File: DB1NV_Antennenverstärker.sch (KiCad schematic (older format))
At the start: 36 parts, among them P1 CONN_01X01_Antenne, P2 CONN_01X02, Q1 BF 545A, Q2 BF 199, Q3 BF 324, U1 LM7812ACT

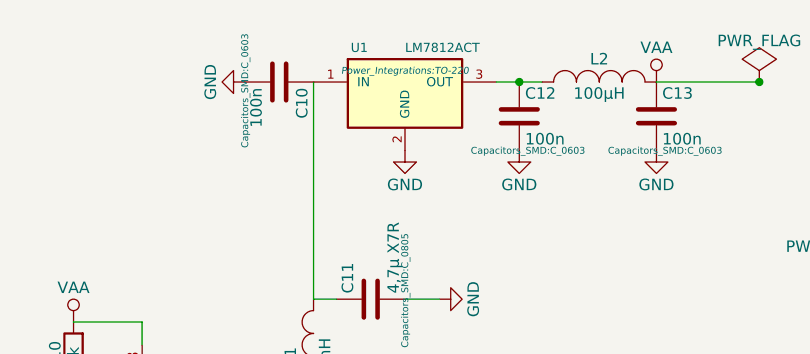
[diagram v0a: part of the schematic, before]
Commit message: Platine v0.1 zum E-Feld Empfänger fertiggestellt.
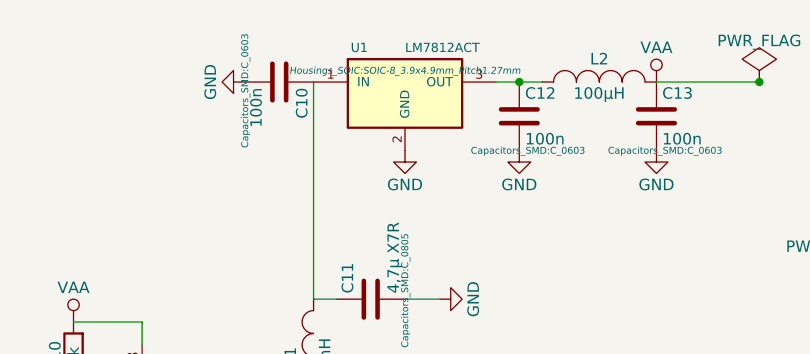
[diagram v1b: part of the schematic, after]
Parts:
- L1, L2: footprint (none) -> lpis2812:L-PIS2812
- U1: footprint Power_Integrations:TO-220 -> Housings_SOIC:SOIC-8_3.9x4.9mm_Pitch1.27mm
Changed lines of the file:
@@
 LIBS:contrib
 LIBS:valves
+LIBS:DB1NV_Antennenverstärker-cache
 EELAYER 25 0
 EELAYER END
@@
 F 0 "L1" H 7750 3700 50  0000 C CNN
 F 1 "1mH" H 7750 3550 50  0000 C CNN
-F 2 "" H 7750 3600 60  0001 C CNN
+F 2 "lpis2812:L-PIS2812" H 7750 3600 60  0001 C CNN
 F 3 "" H 7750 3600 60  0000 C CNN
 F 4 "L-PIS2812" H 7750 3600 60  0001 C CNN "Bauform"
@@
 F 0 "L2" H 9000 2500 50  0000 C CNN
 F 1 "100µH" H 9000 2350 50  0000 C CNN
-F 2 "" H 9000 2400 60  0001 C CNN
+F 2 "lpis2812:L-PIS2812" H 9000 2400 60  0001 C CNN
 F 3 "" H 9000 2400 60  0000 C CNN
 F 4 "L-PIS2812" H 9000 2400 60  0001 C CNN "Bauform"
@@
 F 0 "U1" H 7950 2650 40  0000 C CNN
 F 1 "LM7812ACT" H 8150 2650 40  0000 L CNN
-F 2 "Power_Integrations:TO-220" H 8150 2550 30  0000 C CIN
+F 2 "Housings_SOIC:SOIC-8_3.9x4.9mm_Pitch1.27mm" H 8150 2550 30  0000 C CIN
 F 3 "" H 8150 2450 60  0000 C CNN
 	1    8150 2450
@@
 $EndComp
 $Comp
-L GND #PWR018
+L GND #PWR017
 U 1 1 558375F6
 P 3100 4950
-F 0 "#PWR018" H 3100 4700 50  0001 C CNN
+F 0 "#PWR017" H 3100 4700 50  0001 C CNN
 F 1 "GND" H 3100 4800 50  0000 C CNN
 F 2 "" H 3100 4950 60  0000 C CNN
@@
 $EndComp
 $Comp
-L PWR_FLAG #FLG019
+L PWR_FLAG #FLG018
 U 1 1 55837A31
 P 10000 3300
-F 0 "#FLG019" H 10000 3395 50  0001 C CNN
+F 0 "#FLG018" H 10000 3395 50  0001 C CNN
 F 1 "PWR_FLAG" H 10000 3480 50  0000 C CNN
 F 2 "" H 10000 3300 60  0000 C CNN
@@
 $EndComp
 $Comp
-L GND #PWR020
+L GND #PWR019
 U 1 1 55837AB5
 P 10000 3300
-F 0 "#PWR020" H 10000 3050 50  0001 C CNN
+F 0 "#PWR019" H 10000 3050 50  0001 C CNN
 F 1 "GND" H 10000 3150 50  0000 C CNN
 F 2 "" H 10000 3300 60  0000 C CNN
@@
 $EndComp
 $Comp
-L GND #PWR021
+L GND #PWR020
 U 1 1 55837BE5
 P 8100 4400
-F 0 "#PWR021" H 8100 4150 50  0001 C CNN
+F 0 "#PWR020" H 8100 4150 50  0001 C CNN
 F 1 "GND" H 8100 4250 50  0000 C CNN
 F 2 "" H 8100 4400 60  0000 C CNN
@@
 $EndComp
 $Comp
-L VAA #PWR022
+L VAA #PWR021
 U 1 1 5583806A
 P 9250 2400
-F 0 "#PWR022" H 9250 2250 50  0001 C CNN
+F 0 "#PWR021" H 9250 2250 50  0001 C CNN
 F 1 "VAA" H 9250 2550 50  0000 C CNN
 F 2 "" H 9250 2400 60  0000 C CNN
@@
 $EndComp
 $Comp
-L PWR_FLAG #FLG023
+L PWR_FLAG #FLG022
 U 1 1 5583820C
 P 9700 2400
-F 0 "#FLG023" H 9700 2495 50  0001 C CNN
+F 0 "#FLG022" H 9700 2495 50  0001 C CNN
 F 1 "PWR_FLAG" H 9700 2580 50  0000 C CNN
 F 2 "" H 9700 2400 60  0000 C CNN

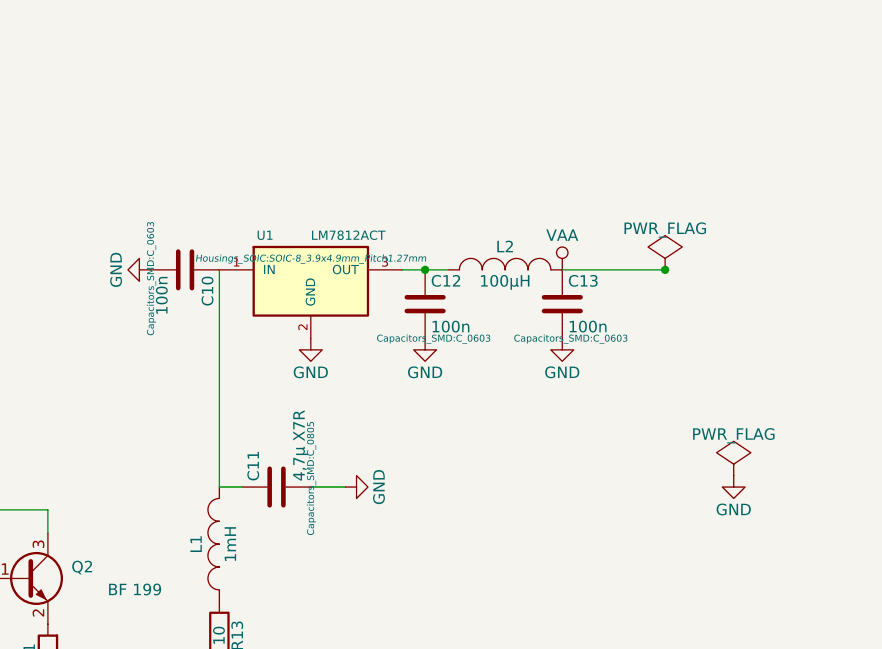
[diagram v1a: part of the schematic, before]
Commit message: Hinzufügen des LT3042 zum Schaltplan (Werte der externen Beschaltung noch nicht berechnet)
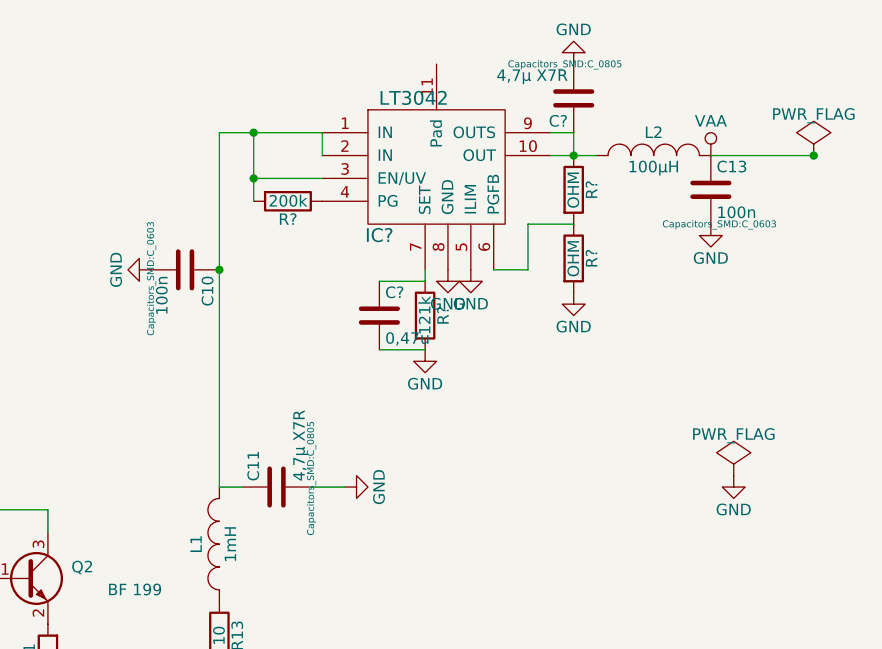
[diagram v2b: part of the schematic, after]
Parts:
- removed C12: 100n, Capacitors_SMD:C_0603, symbol C
- removed U1: LM7812ACT, Housings_SOIC:SOIC-8_3.9x4.9mm_Pitch1.27mm, symbol LM7812ACT
- added C?: 0,47u, symbol C
- added C?: 4,7µ X7R, Capacitors_SMD:C_0805, symbol C
- added IC?: LT3042, symbol LT3042
- added R?: 200k, symbol R
- added R?: 121k, symbol R
- added R? (x2): OHM, symbol R
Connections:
- net GND: now also C?.2, C?.2, IC?.5 (ILIM), IC?.8 (GND), R?.2, R?.2
- net at C10.1, C11.1, L1.2: now also IC?.1 (IN), IC?.2 (IN), IC?.3 (EN/UV), R?.2
- net at L2.1: now also C?.1, IC?.10 (OUT), IC?.9 (OUTS), R?.1
- new net: IC?.4 (PG), R?.1
- new net: IC?.6 (PGFB), R?.1, R?.2
- new net: C?.1, IC?.7 (SET), R?.1
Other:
- moved on the sheet: C13, L2

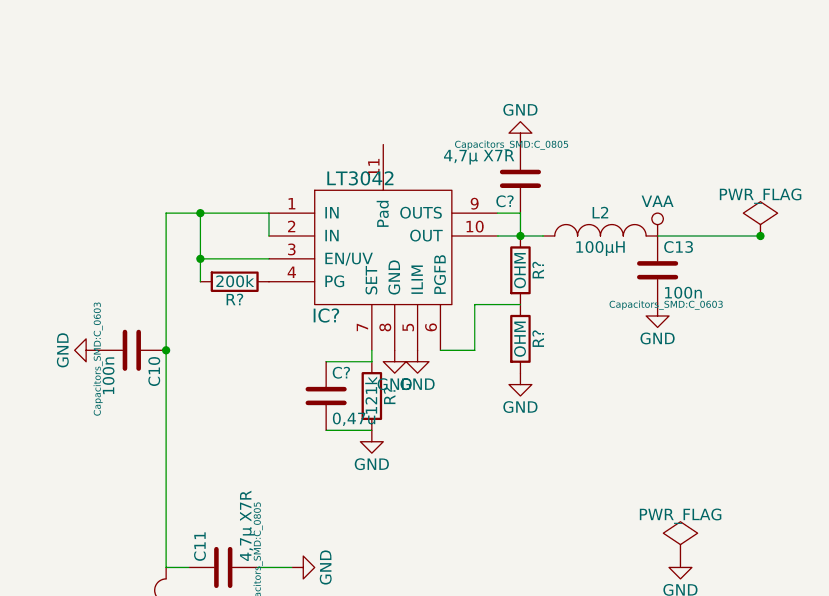
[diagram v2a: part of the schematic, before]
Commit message: Anpassung der Werte des LT3042 Optimierung für Minimales Rauschen (längeres Startup) Undervoltage Threshold  = 10.02 V Power Good Threshold = 11.8 V
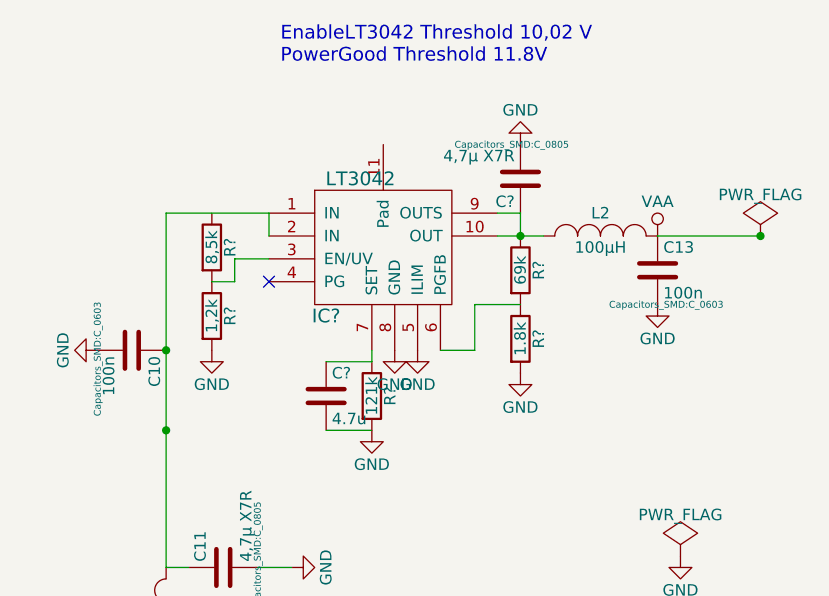
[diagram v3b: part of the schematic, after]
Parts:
- removed R?: 200k, symbol R
- added R?: 1,2k, symbol R
- added R?: 8,5k, symbol R
- C?: value 0,47u -> 4.7u
- R?: value OHM -> 69k
- R?: value OHM -> 1.8k
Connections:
- net GND: now also R?.2
- net at C10.1, C11.1, IC?.1 (IN)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: no longer IC?.3 (EN/UV)
- new net: IC?.3 (EN/UV), R?.1, R?.2
- no-connect marks 0 -> 1
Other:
- note added: "EnableLT3042 Threshold 10,02 V\nPowerGood Threshold 11.8V"
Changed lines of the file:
@@
 Connection ~ 7750 2400
-$Comp
-L R R?
-U 1 1 558D7F66
-P 8050 2100
-F 0 "R?" V 8130 2100 50  0000 C CNN
-F 1 "200k" V 8050 2100 50  0000 C CNN
-F 2 "" V 7980 2100 30  0000 C CNN
-F 3 "" H 8050 2100 30  0000 C CNN
-	1    8050 2100
-	0    1    1    0
-$EndComp
-Wire Wire Line
-	8200 2000 7900 2000
-Wire Wire Line
-	7900 1800 7900 2100
-Connection ~ 7900 1800
-Connection ~ 7900 2000
 $Comp
 L GND #PWR?
@@
 P 8450 2600
 F 0 "C?" H 8475 2700 50  0000 L CNN
-F 1 "0,47u" H 8475 2500 50  0000 L CNN
+F 1 "4.7u" H 8475 2500 50  0000 L CNN
 F 2 "" H 8488 2450 30  0000 C CNN
 F 3 "" H 8450 2600 60  0000 C CNN
@@
 P 9300 2050
 F 0 "R?" V 9380 2050 50  0000 C CNN
-F 1 "OHM" V 9300 2050 50  0000 C CNN
+F 1 "69k" V 9300 2050 50  0000 C CNN
 F 2 "" V 9230 2050 30  0000 C CNN
 F 3 "" H 9300 2050 30  0000 C CNN
@@
 P 9300 2350
 F 0 "R?" V 9380 2350 50  0000 C CNN
-F 1 "OHM" V 9300 2350 50  0000 C CNN
+F 1 "1.8k" V 9300 2350 50  0000 C CNN
 F 2 "" V 9230 2350 30  0000 C CNN
 F 3 "" H 9300 2350 30  0000 C CNN
@@
 Wire Wire Line
 	9100 2400 8950 2400
+$Comp
+L R R?
+U 1 1 558E5880
+P 7950 2250
+F 0 "R?" V 8030 2250 50  0000 C CNN
+F 1 "1,2k" V 7950 2250 50  0000 C CNN
+F 2 "" V 7880 2250 30  0000 C CNN
+F 3 "" H 7950 2250 30  0000 C CNN
+	1    7950 2250
+	1    0    0    -1
+$EndComp
+$Comp
+L R R?
+U 1 1 558E5960
+P 7950 1950
+F 0 "R?" V 8030 1950 50  0000 C CNN
+F 1 "8,5k" V 7950 1950 50  0000 C CNN
+F 2 "" V 7880 1950 30  0000 C CNN
+F 3 "" H 7950 1950 30  0000 C CNN
+	1    7950 1950
+	1    0    0    -1
+$EndComp
+$Comp
+L GND #PWR?
+U 1 1 558E5B71
+P 7950 2400
+F 0 "#PWR?" H 7950 2150 50  0001 C CNN
+F 1 "GND" H 7950 2250 50  0000 C CNN
+F 2 "" H 7950 2400 60  0000 C CNN
+F 3 "" H 7950 2400 60  0000 C CNN
+	1    7950 2400
+	1    0    0    -1
+$EndComp
+Wire Wire Line
+	7950 2100 8050 2100
+Wire Wire Line
+	8050 2100 8050 2000
+Wire Wire Line
+	8050 2000 8200 2000
+Connection ~ 7750 2750
+NoConn ~ 8200 2100
+Text Notes 8250 1150 0    60   ~ 0
+EnableLT3042 Threshold 10,02 V\nPowerGood Threshold 11.8V
 $EndSCHEMATC

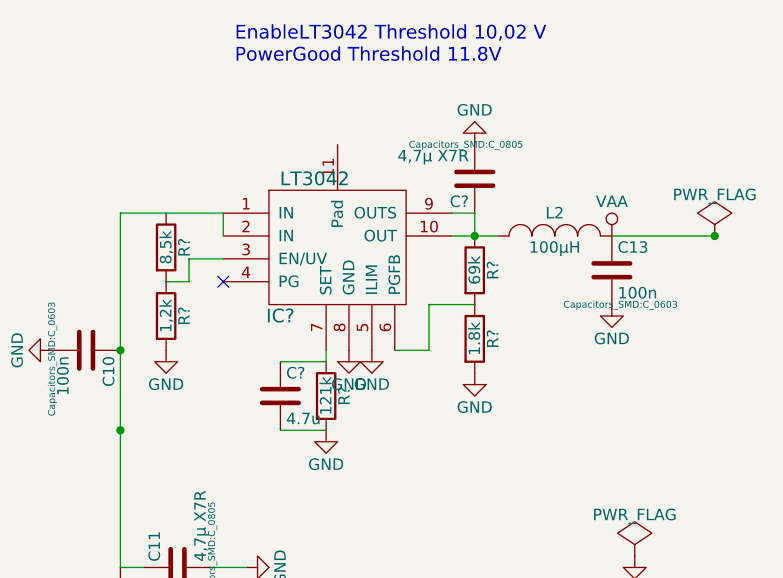
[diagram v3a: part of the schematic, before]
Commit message: Schaltplan leicht modifiziert. eine Spule weniger
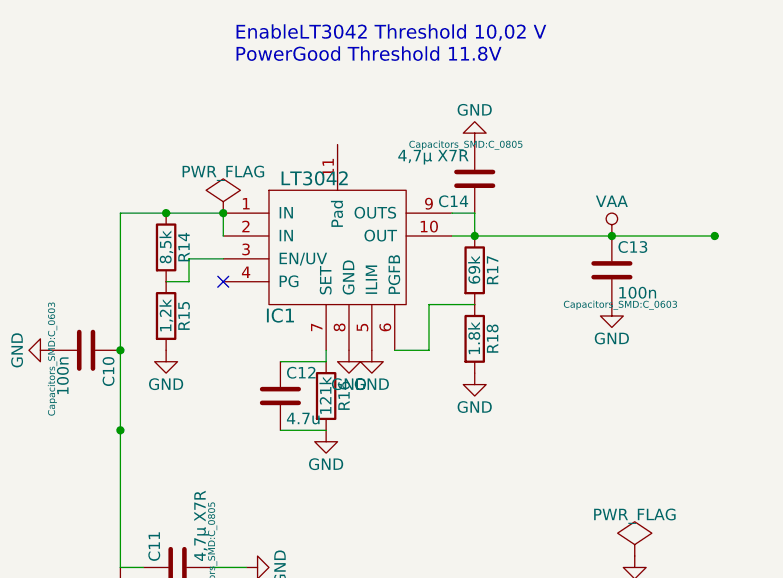
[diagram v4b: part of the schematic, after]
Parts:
- removed L2: 100µH, lpis2812:L-PIS2812, symbol INDUCTOR_SMALL
- gave numbers to parts that had none: 8
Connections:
- net VAA: now also C14.1, IC1.10 (OUT), IC1.9 (OUTS), R17.1
- net at C10.1, C11.1, IC1.1 (IN)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: now also R14.1
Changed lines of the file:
@@
-$EndComp
-$Comp
-L INDUCTOR_SMALL L2
-U 1 1 558344EB
-P 9650 1900
-F 0 "L2" H 9650 2000 50  0000 C CNN
-F 1 "100µH" H 9650 1850 50  0000 C CNN
-F 2 "lpis2812:L-PIS2812" H 9650 1900 60  0001 C CNN
-F 3 "" H 9650 1900 60  0000 C CNN
-F 4 "L-PIS2812" H 9650 1900 60  0001 C CNN "Bauform"
-	1    9650 1900
-	1    0    0    -1
 $EndComp
 $Comp
@@
 $EndComp
 Wire Wire Line
-	9200 1900 9400 1900
+	9200 1900 10350 1900
 Connection ~ 9300 1900
 $Comp
-L GND #PWR015
+L GND #PWR013
 U 1 1 55834F27
 P 7450 2400
-F 0 "#PWR015" H 7450 2150 50  0001 C CNN
+F 0 "#PWR013" H 7450 2150 50  0001 C CNN
 F 1 "GND" H 7450 2250 50  0000 C CNN
 F 2 "" H 7450 2400 60  0000 C CNN
@@
 $EndComp
 $Comp
-L GND #PWR016
+L GND #PWR014
 U 1 1 55835498
 P 9900 2200
-F 0 "#PWR016" H 9900 1950 50  0001 C CNN
+F 0 "#PWR014" H 9900 1950 50  0001 C CNN
 F 1 "GND" H 9900 2050 50  0000 C CNN
 F 2 "" H 9900 2200 60  0000 C CNN
@@
 	1    0    0    -1
 $EndComp
-Wire Wire Line
-	9900 1900 10350 1900
 $Comp
 L ZENER D1
@@
 $EndComp
 $Comp
-L GND #PWR017
+L GND #PWR015
 U 1 1 558375F6
 P 3100 4950
-F 0 "#PWR017" H 3100 4700 50  0001 C CNN
+F 0 "#PWR015" H 3100 4700 50  0001 C CNN
 F 1 "GND" H 3100 4800 50  0000 C CNN
 F 2 "" H 3100 4950 60  0000 C CNN
@@
 $EndComp
 $Comp
-L PWR_FLAG #FLG018
+L PWR_FLAG #FLG016
 U 1 1 55837A31
 P 10000 3300
-F 0 "#FLG018" H 10000 3395 50  0001 C CNN
+F 0 "#FLG016" H 10000 3395 50  0001 C CNN
 F 1 "PWR_FLAG" H 10000 3480 50  0000 C CNN
 F 2 "" H 10000 3300 60  0000 C CNN
@@
 $EndComp
 $Comp
-L GND #PWR019
+L GND #PWR017
 U 1 1 55837AB5
 P 10000 3300
-F 0 "#PWR019" H 10000 3050 50  0001 C CNN
+F 0 "#PWR017" H 10000 3050 50  0001 C CNN
 F 1 "GND" H 10000 3150 50  0000 C CNN
 F 2 "" H 10000 3300 60  0000 C CNN
@@
 $EndComp
 $Comp
-L GND #PWR020
+L GND #PWR018
 U 1 1 55837BE5
 P 8100 4400
-F 0 "#PWR020" H 8100 4150 50  0001 C CNN
+F 0 "#PWR018" H 8100 4150 50  0001 C CNN
 F 1 "GND" H 8100 4250 50  0000 C CNN
 F 2 "" H 8100 4400 60  0000 C CNN
@@
 $EndComp
 $Comp
-L VAA #PWR021
+L VAA #PWR019
 U 1 1 5583806A
 P 9900 1900
-F 0 "#PWR021" H 9900 1750 50  0001 C CNN
+F 0 "#PWR019" H 9900 1750 50  0001 C CNN
 F 1 "VAA" H 9900 2050 50  0000 C CNN
 F 2 "" H 9900 1900 60  0000 C CNN
@@
 	1    0    0    -1
 $EndComp
-$Comp
-L PWR_FLAG #FLG022
-U 1 1 5583820C
-P 10350 1900
-F 0 "#FLG022" H 10350 1995 50  0001 C CNN
-F 1 "PWR_FLAG" H 10350 2080 50  0000 C CNN
-F 2 "" H 10350 1900 60  0000 C CNN
-F 3 "" H 10350 1900 60  0000 C CNN
-	1    10350 1900
-	1    0    0    -1
-$EndComp
 Connection ~ 10350 1900
 $Comp
-L LT3042 IC?
+L LT3042 IC1
 U 1 1 558D77FE
 P 8700 1950
-F 0 "IC?" H 8450 1650 60  0000 C CNN
+F 0 "IC1" H 8450 1650 60  0000 C CNN
 F 1 "LT3042" H 8600 2250 60  0000 C CNN
-F 2 "" H 8950 1950 60  0000 C CNN
+F 2 "" H 8950 1950 60  0001 C CNN
 F 3 "" H 8950 1950 60  0000 C CNN
 	1    8700 1950
@@
 $EndComp
 Wire Wire Line
-	8200 1900 8200 1800
-Wire Wire Line
 	8200 1800 7750 1800
 Connection ~ 7750 2400
 $Comp
-L GND #PWR?
+L GND #PWR020
 U 1 1 558D8129
 P 8650 2750
-F 0 "#PWR?" H 8650 2500 50  0001 C CNN
+F 0 "#PWR020" H 8650 2500 50  0001 C CNN
 F 1 "GND" H 8650 2600 50  0000 C CNN
 F 2 "" H 8650 2750 60  0000 C CNN
@@
 $EndComp
 $Comp
-L R R?
+L R R16
 U 1 1 558D81AD
 P 8650 2600
-F 0 "R?" V 8730 2600 50  0000 C CNN
+F 0 "R16" V 8730 2600 50  0000 C CNN
 F 1 "121k" V 8650 2600 50  0000 C CNN
-F 2 "" V 8580 2600 30  0000 C CNN
+F 2 "" V 8580 2600 30  0001 C CNN
 F 3 "" H 8650 2600 30  0000 C CNN
 	1    8650 2600
@@
 $EndComp
 $Comp
-L C C?
+L C C12
 U 1 1 558D8228
 P 8450 2600
-F 0 "C?" H 8475 2700 50  0000 L CNN
+F 0 "C12" H 8475 2700 50  0000 L CNN
 F 1 "4.7u" H 8475 2500 50  0000 L CNN
-F 2 "" H 8488 2450 30  0000 C CNN
+F 2 "" H 8488 2450 30  0001 C CNN
 F 3 "" H 8450 2600 60  0000 C CNN
 	1    8450 2600
@@
 	8650 2450 8650 2400
 $Comp
-L GND #PWR?
+L GND #PWR021
 U 1 1 558D85A4
 P 8750 2400
-F 0 "#PWR?" H 8750 2150 50  0001 C CNN
+F 0 "#PWR021" H 8750 2150 50  0001 C CNN
 F 1 "GND" H 8750 2250 50  0000 C CNN
 F 2 "" H 8750 2400 60  0000 C CNN
@@
 $EndComp
 $Comp
-L GND #PWR?
+L GND #PWR022
 U 1 1 558D8624
 P 8850 2400
-F 0 "#PWR?" H 8850 2150 50  0001 C CNN
+F 0 "#PWR022" H 8850 2150 50  0001 C CNN
 F 1 "GND" H 8850 2250 50  0000 C CNN
 F 2 "" H 8850 2400 60  0000 C CNN
@@
 	9300 1800 9300 1900
 $Comp
-L C C?
+L C C14
 U 1 1 558D886A
 P 9300 1650
-F 0 "C?" H 9325 1750 50  0000 L CNN
+F 0 "C14" H 9325 1750 50  0000 L CNN
 F 1 "4,7µ X7R" H 9325 1550 50  0000 L CNN
 F 2 "Capacitors_SMD:C_0805" H 9338 1500 30  0000 C CNN
@@
 $EndComp
 $Comp
-L GND #PWR?
+L GND #PWR023
 U 1 1 558D8A3B
 P 9300 1500
-F 0 "#PWR?" H 9300 1250 50  0001 C CNN
+F 0 "#PWR023" H 9300 1250 50  0001 C CNN
 F 1 "GND" H 9300 1350 50  0000 C CNN
 F 2 "" H 9300 1500 60  0000 C CNN
@@
 $EndComp
 $Comp
-L R R?
+L R R17
 U 1 1 558D8BDF
 P 9300 2050
-F 0 "R?" V 9380 2050 50  0000 C CNN
+F 0 "R17" V 9380 2050 50  0000 C CNN
 F 1 "69k" V 9300 2050 50  0000 C CNN
-F 2 "" V 9230 2050 30  0000 C CNN
+F 2 "" V 9230 2050 30  0001 C CNN
 F 3 "" H 9300 2050 30  0000 C CNN
 	1    9300 2050
@@
 $EndComp
 $Comp
-L R R?
+L R R18
 U 1 1 558D8C78
 P 9300 2350
-F 0 "R?" V 9380 2350 50  0000 C CNN
+F 0 "R18" V 9380 2350 50  0000 C CNN
 F 1 "1.8k" V 9300 2350 50  0000 C CNN
-F 2 "" V 9230 2350 30  0000 C CNN
+F 2 "" V 9230 2350 30  0001 C CNN
 F 3 "" H 9300 2350 30  0000 C CNN
 	1    9300 2350
@@
 $EndComp
 $Comp
-L GND #PWR?
+L GND #PWR024
 U 1 1 558D8D1A
 P 9300 2500
-F 0 "#PWR?" H 9300 2250 50  0001 C CNN
+F 0 "#PWR024" H 9300 2250 50  0001 C CNN
 F 1 "GND" H 9300 2350 50  0000 C CNN
 F 2 "" H 9300 2500 60  0000 C CNN
@@
 	9100 2400 8950 2400
 $Comp
-L R R?
+L R R15
 U 1 1 558E5880
 P 7950 2250
-F 0 "R?" V 8030 2250 50  0000 C CNN
+F 0 "R15" V 8030 2250 50  0000 C CNN
 F 1 "1,2k" V 7950 2250 50  0000 C CNN
-F 2 "" V 7880 2250 30  0000 C CNN
+F 2 "" V 7880 2250 30  0001 C CNN
 F 3 "" H 7950 2250 30  0000 C CNN
 	1    7950 2250
@@
 $EndComp
 $Comp
-L R R?
+L R R14
 U 1 1 558E5960
 P 7950 1950
-F 0 "R?" V 8030 1950 50  0000 C CNN
+F 0 "R14" V 8030 1950 50  0000 C CNN
 F 1 "8,5k" V 7950 1950 50  0000 C CNN
-F 2 "" V 7880 1950 30  0000 C CNN
+F 2 "" V 7880 1950 30  0001 C CNN
 F 3 "" H 7950 1950 30  0000 C CNN
 	1    7950 1950
@@
 $EndComp
 $Comp
-L GND #PWR?
+L GND #PWR025
 U 1 1 558E5B71
 P 7950 2400
-F 0 "#PWR?" H 7950 2150 50  0001 C CNN
+F 0 "#PWR025" H 7950 2150 50  0001 C CNN
 F 1 "GND" H 7950 2250 50  0000 C CNN
 F 2 "" H 7950 2400 60  0000 C CNN
@@
 Text Notes 8250 1150 0    60   ~ 0
 EnableLT3042 Threshold 10,02 V\nPowerGood Threshold 11.8V
+Connection ~ 9900 1900
+Connection ~ 8200 1800
+Connection ~ 7950 1800
+Wire Wire Line
+	8200 1900 8200 1800
+$Comp
+L PWR_FLAG #FLG026
+U 1 1 558E715F
+P 8200 1800
+F 0 "#FLG026" H 8200 1895 50  0001 C CNN
+F 1 "PWR_FLAG" H 8200 1980 50  0000 C CNN
+F 2 "" H 8200 1800 60  0000 C CNN
+F 3 "" H 8200 1800 60  0000 C CNN
+	1    8200 1800
+	1    0    0    -1
+$EndComp
 $EndSCHEMATC
